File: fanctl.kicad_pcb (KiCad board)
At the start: 4 copper layers, 37.8 x 25 mm, 28 parts, among them U1 74LVC2G17, U2 74LVC2G17

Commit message: release candidate
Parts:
- removed R1, R2, R3: 0R, Resistor_SMD:R_0603_1608Metric_Pad0.98x0.95mm_HandSolder
- removed RPI1: Conn_01x05, Connector_PinHeader_2.54mm:PinHeader_1x05_P2.54mm_Horizontal
- removed SUP1: Conn_01x02, Connector_PinHeader_2.54mm:PinHeader_1x02_P2.54mm_Horizontal
- added D8: LTST-C191TBKT, Diode_SMD:D_0402_1005Metric_Pad0.77x0.64mm_HandSolder, F.Cu at (81.8, 77.0)
- added J1: Raspberry_Pi_4, Connector_PinSocket_2.54mm:PinSocket_2x20_P2.54mm_Horizontal, F.Cu at (35.1, 87.4)
- added J4: Raspberry_Pi_4, Connector_PinHeader_2.54mm:PinHeader_2x20_P2.54mm_Vertical, F.Cu at (35.1, 83.8)
- added R13: 510K, Resistor_SMD:R_0603_1608Metric_Pad0.98x0.95mm_HandSolder, F.Cu at (69.8, 77.0)
- added R14: 0R, Resistor_SMD:R_0603_1608Metric_Pad0.98x0.95mm_HandSolder, F.Cu at (75.8, 77.0)
- added R15: 0R, Resistor_SMD:R_0603_1608Metric_Pad0.98x0.95mm_HandSolder, F.Cu at (72.8, 77.0)
- added R16: 1K, Resistor_SMD:R_0603_1608Metric_Pad0.98x0.95mm_HandSolder, F.Cu at (78.8, 77.0)
- added R18: 0R, Resistor_SMD:R_0603_1608Metric_Pad0.98x0.95mm_HandSolder, F.Cu at (45.8, 77.0)
- added R19: 0R, Resistor_SMD:R_0603_1608Metric_Pad0.98x0.95mm_HandSolder, F.Cu at (42.8, 77.0)
- C1, C2: footprint Capacitor_SMD:C_0603_1608Metric_Pad1.08x0.95mm_HandSolder -> Capacitor_SMD:C_0805_2012Metric_Pad1.18x1.45mm_HandSolder
- G***: moved to F.Cu
- U1, U2: value 74LVC2G17 -> SN74HCT125DR; footprint Package_TO_SOT_SMD:SOT-23-6_Handsoldering -> Package_SO:SOIC-14_3.9x8.7mm_P1.27mm
- moved G*** 81.7 mm to (68.2, 46.0), turned to 0 degrees
- moved FAN1 74.6 mm to (38.0, 47.8), turned to 180 degrees
- moved FAN2 74.5 mm to (38.1, 60.0), turned to 180 degrees
- moved D4 65.0 mm to (42.8, 59.0), turned to -90 degrees
- moved D6 65.0 mm to (42.8, 52.0), turned to 180 degrees
- moved D1 64.9 mm to (42.8, 47.0), turned to -90 degrees
- moved D5 64.8 mm to (42.8, 40.0), turned to 180 degrees
- moved R9 62.7 mm to (47.8, 52.0), turned to 180 degrees
- moved R6 62.4 mm to (47.8, 40.0), turned to 180 degrees
- moved C1 60.2 mm to (47.8, 47.0), turned to -90 degrees
- moved R7 59.2 mm to (42.8, 43.0), turned to 0 degrees
- moved C2 57.4 mm to (47.8, 59.0), turned to -90 degrees
- moved R10 57.0 mm to (42.8, 55.0), turned to 0 degrees
- moved D2 56.9 mm to (42.8, 67.0)
- moved R8 56.9 mm to (47.8, 43.0), turned to 0 degrees
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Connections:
- U1 pad 1: PWM_CTL_3V3 -> GND
- U1 pad 2: GND -> PWM_FAN_CTL_3V3
- U1 pad 3: GND -> PWM_CTL_5V
- U1 pad 4: unconnected-(U1-Pad4) -> GND
- U1 pad 5: +5V -> PWM0_3V3
- U1 pad 6: PWM_CTL_5V -> Net-(R16-Pad1)
- U2 pad 1: Net-(R10-Pad2) -> GND
- U2 pad 2: GND -> Net-(R7-Pad2)
- U2 pad 3: Net-(R7-Pad2) -> TACH1_3V3
- U2 pad 4: TACH1_3V3 -> GND
- U2 pad 5: +3.3V -> Net-(R10-Pad2)
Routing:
- net +3.3V: track 17.8 -> 131.6 mm, vias 1 -> 3
- net GND: track 25.4 -> 109.2 mm, vias 46 -> 81
- net PWM_CTL_3V3: track 35.9 -> 0.00 mm
- net +5V: track 82.0 -> 115.3 mm, vias 6 -> 2
- net PWM_CTL_5V: track 45.3 -> 71.5 mm, vias 0 -> 3
- net TACH1_3V3: track 30.2 -> 50.4 mm
- net TACH2_5V: track 18.4 -> 3.59 mm
- net TACH1_5V: track 18.1 -> 4.29 mm
- net Net-(J1-GPIO15/UART_RXD): track 0.00 -> 13.3 mm
- net Net-(J1-GPIO12/PWM0): track 0.00 -> 13.3 mm
- net Net-(J1-GPIO14/UART_TXD): track 0.00 -> 13.3 mm
- net PWM_FAN_CTL_3V3: track 0.00 -> 11.3 mm
- net Net-(J1-GPIO13/PWM1): track 0.00 -> 10.7 mm
- net Net-(J1-GPIO20/SPI1_MOSI/PCM_DIN/PWM1): track 0.00 -> 9.62 mm
- net Net-(J1-~{CE0}_SPI0/GPIO08): track 0.00 -> 9.62 mm
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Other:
- board size 37.8 x 25 mm -> 51 x 64 mm
- board text added: "${TITLE} ${REVISION} 01/25 5V FANS ONLY"
- board text added: "CTL"
- board text added: "PWR"
- board text removed: "5V"
- board text removed: "5V FANS"
- board text removed: "PWM"
- board text removed: "rPi_fan_ctl v0.1.1 01/25"
- board text removed: "regensberry"

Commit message: review feedback
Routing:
- net PWM_CTL_5V: track 71.5 -> 72.0 mm
- net GND: vias 81 -> 82
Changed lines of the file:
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@@
 		(title "rPi-fanctl")
 		(date "2025-01-18")
-		(rev "v0.2.0")
+		(rev "v0.2.1")
 	)
 	(layers
@@
 		)
 		(property "Value" "1K"
-			(at 0 1.43 360)
+			(at 0 1.43 0)
 			(layer "F.Fab")
 			(effects
@@
 		)
 		(fp_text user "${REFERENCE}"
-			(at 0 0 360)
+			(at 0 0 0)
 			(layer "F.Fab")
 			(effects
@@
 		)
 		(property "Value" "Conn_01x04"
-			(at 4.385 9.89 360)
+			(at 4.385 9.89 0)
 			(layer "F.Fab")
 			(effects
@@
 		)
 		(property "Value" "1K"
-			(at 0 1.43 360)
+			(at 0 1.43 0)
 			(layer "F.Fab")
 			(effects
@@
 		)
 		(fp_text user "${REFERENCE}"
-			(at 0 0 360)
+			(at 0 0 0)
 			(layer "F.Fab")
 			(effects
@@
 		(tags "resistor handsolder")
 		(property "Reference" "R11"
-			(at 0 -1.43 360)
+			(at 0 -1.43 0)
 			(layer "F.SilkS")
 			(effects
@@
 		)
 		(property "Value" "33K"
-			(at 0 1.43 360)
+			(at 0 1.43 0)
 			(layer "F.Fab")
 			(effects
@@
 		)
 		(fp_text user "${REFERENCE}"
-			(at 0 0 360)
+			(at 0 0 0)
 			(layer "F.Fab")
 			(effects
@@
 		)
 		(property "Value" "0u1"
-			(at 0 1.43 360)
+			(at 0 1.43 0)
 			(layer "F.Fab")
 			(effects
@@
 		)
 		(fp_text user "${REFERENCE}"
-			(at 0 0 360)
+			(at 0 0 0)
 			(layer "F.Fab")
 			(effects
@@
 		(tags "resistor handsolder")
 		(property "Reference" "R4"
-			(at 0 -1.43 360)
+			(at 0 -1.43 0)
 			(layer "F.SilkS")
 			(effects
@@
 		)
 		(property "Value" "1K"
-			(at 0 1.43 360)
+			(at 0 1.43 0)
 			(layer "F.Fab")
 			(effects
@@
 		)
 		(fp_text user "${REFERENCE}"
-			(at 0 0 360)
+			(at 0 0 0)
 			(layer "F.Fab")
 			(effects
@@
 		)
 		(property "Value" "LTST-C191TBKT"
-			(at 0 1.17 360)
+			(at 0 1.17 0)
 			(layer "F.Fab")
 			(effects
@@
 		)
 		(fp_text user "${REFERENCE}"
-			(at 0 0 360)
+			(at 0 0 0)
 			(layer "F.Fab")
 			(effects
@@
 		(tags "resistor handsolder")
 		(property "Reference" "R10"
-			(at 0 -1.43 360)
+			(at 0 -1.43 0)
 			(layer "F.SilkS")
 			(effects
@@
 		)
 		(property "Value" "18K"
-			(at 0 1.43 360)
+			(at 0 1.43 0)
 			(layer "F.Fab")
 			(effects
@@
 		)
 		(fp_text user "${REFERENCE}"
-			(at 0 0 360)
+			(at 0 0 0)
 			(layer "F.Fab")
 			(effects
@@
 		(tags "Through hole angled socket strip THT 2x20 2.54mm double row")
 		(property "Reference" "J1"
-			(at -5.65 -2.77 90)
+			(at -7.54 2.5 90)
 			(layer "F.SilkS")
 			(effects
@@
 		)
 		(fp_text user "${REFERENCE}"
-			(at -8.315 24.13 360)
+			(at -8.315 24.13 0)
 			(layer "F.Fab")
 			(effects
@@
 		(tags "Through hole pin header THT 2x20 2.54mm double row")
 		(property "Reference" "J4"
-			(at 1.27 -2.33 90)
+			(at -8.96 2.6 90)
 			(layer "F.SilkS")
 			(effects
@@
 		)
 		(fp_text user "${REFERENCE}"
-			(at 1.27 24.13 360)
+			(at 1.27 24.13 0)
 			(layer "F.Fab")
 			(effects
@@
 		)
 		(property "Value" "Conn_01x04"
-			(at 4.385 9.89 360)
+			(at 4.385 9.89 0)
 			(layer "F.Fab")
 			(effects
@@
 		(tags "diode handsolder")
 		(property "Reference" "D2"
-			(at 0 -1.17 360)
+			(at 0 -1.17 0)
 			(layer "F.SilkS")
 			(effects
@@
 		)
 		(property "Value" "LTST-C191TBKT"
-			(at 0 1.17 360)
+			(at 0 1.17 0)
 			(layer "F.Fab")
 			(effects
@@
 		)
 		(fp_text user "${REFERENCE}"
-			(at 0 0 360)
+			(at 0 0 0)
 			(layer "F.Fab")
 			(effects
@@
 		)
 		(property "Value" "LTST-C191TBKT"
-			(at 0 1.17 360)
+			(at 0 1.17 0)
 			(layer "F.Fab")
 			(effects
@@
 		)
 		(fp_text user "${REFERENCE}"
-			(at 0 0 360)
+			(at 0 0 0)
 			(layer "F.Fab")
 			(effects
@@
 		(tags "SOIC SO")
 		(property "Reference" "U2"
-			(at 0 -5.28 360)
+			(at 0 -5.28 0)
 			(layer "F.SilkS")
 			(effects
@@
 		)
 		(property "Value" "SN74HCT125DR"
-			(at 0 5.28 360)
+			(at 0 5.28 0)
 			(layer "F.Fab")
 			(effects
@@
 		)
 		(property "Footprint" "Package_SO:SOIC-14_3.9x8.7mm_P1.27mm"
-			(at 0 0 360)
+			(at 0 0 0)
 			(layer "F.Fab")
 			(hide yes)
@@
 		)
 		(property "Datasheet" "https://www.ti.com/general/docs/suppproductinfo.tsp?distId=10&gotoUrl=https%3A%2F%2Fwww.ti.com%2Flit%2Fgpn%2Fsn74hct125"
-			(at 0 0 360)
+			(at 0 0 0)
 			(layer "F.Fab")
 			(hide yes)
@@
 		)
 		(property "Description" "IC BUF NON-INVERT 5.5V 14SOIC"
-			(at 0 0 360)
+			(at 0 0 0)
 			(layer "F.Fab")
 			(hide yes)
@@
 		)
 		(fp_text user "${REFERENCE}"
-			(at 0 0 360)
+			(at 0 0 0)
 			(layer "F.Fab")
 			(effects
@@
 	)
 	(via
-		(at 40.25 44)
-		(size 0.8)
-		(drill 0.4)
-		(layers "F.Cu" "B.Cu")
-		(free yes)
-		(net 1)
-	)
-	(via
 		(at 71.25 70.5)
 		(size 0.8)
@@
 	)
 	(via
-		(at 45.25 44)
+		(at 45.25 44.1)
 		(size 0.8)
 		(drill 0.4)
@@
 	)
 	(via
-		(at 61.25 71)
+		(at 74.25 79)
+		(size 0.8)
+		(drill 0.4)
+		(layers "F.Cu" "B.Cu")
+		(free yes)
+		(net 1)
+	)
+	(via
+		(at 60.25 70.5)
 		(size 0.8)
 		(drill 0.4)
@@
 	)
 	(via
-		(at 40.25 56)
+		(at 40.25 44.1)
 		(size 0.8)
 		(drill 0.4)
@@
 	)
 	(via
+		(at 68.15 78.3)
+		(size 0.8)
+		(drill 0.4)
+		(layers "F.Cu" "B.Cu")
+		(free yes)
+		(net 1)
+	)
+	(via
 		(at 58.75 75)
 		(size 0.8)
@@
 	)
 	(segment
-		(start 40.75 72)
-		(end 46.25 72)
-		(width 0.25)
-		(layer "F.Cu")
-		(net 5)
-	)
-	(segment
 		(start 41.8375 65)
 		(end 40.25 65)
@@
 	)
 	(segment
-		(start 40.25 65.5)
-		(end 40.25 71.5)
+		(start 40.75 72)
+		(end 46.25 72)
 		(width 0.25)
 		(layer "F.Cu")
@@
 		(width 0.25)
 		(layer "F.Cu")
+		(net 5)
+	)
+	(segment
+		(start 40.25 65)
+		(end 40.25 71.5)
+		(width 0.25)
+		(layer "F.Cu")

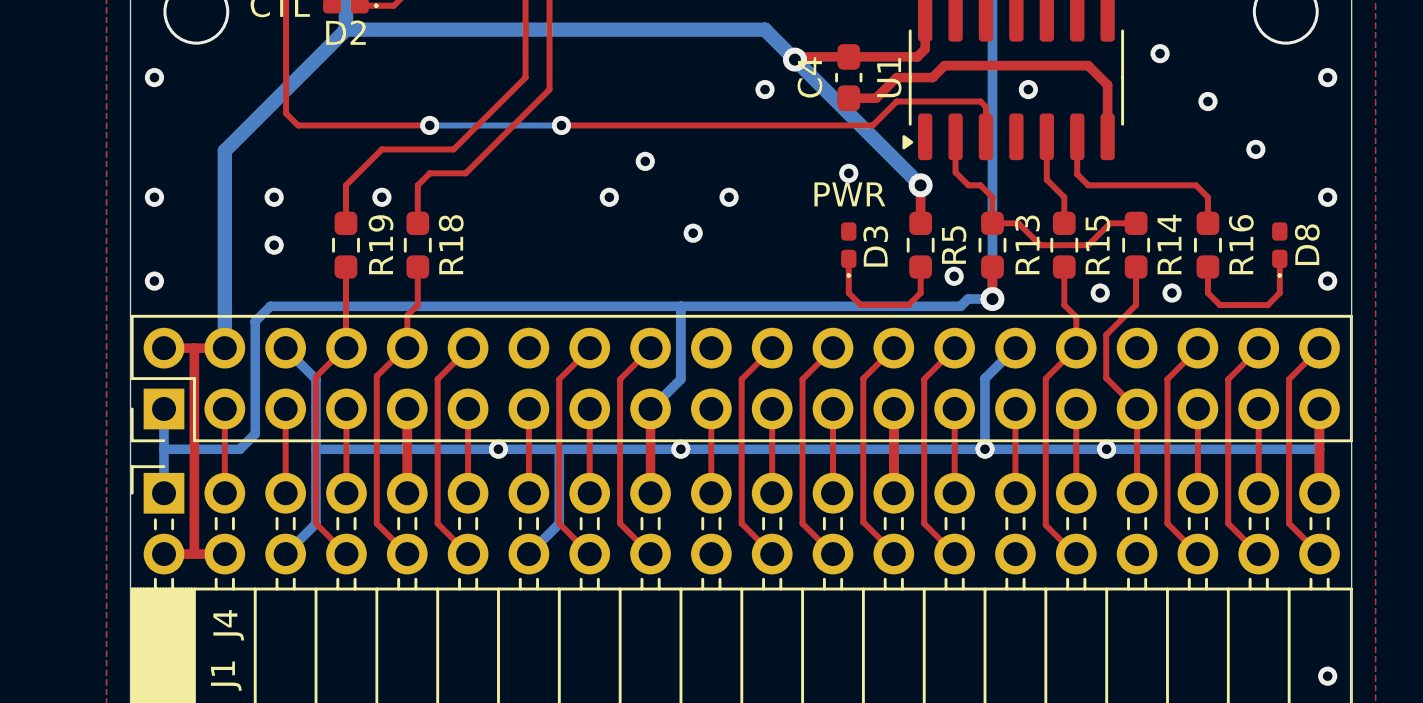
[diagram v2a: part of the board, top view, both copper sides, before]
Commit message: rotated pin headers so they are actually right
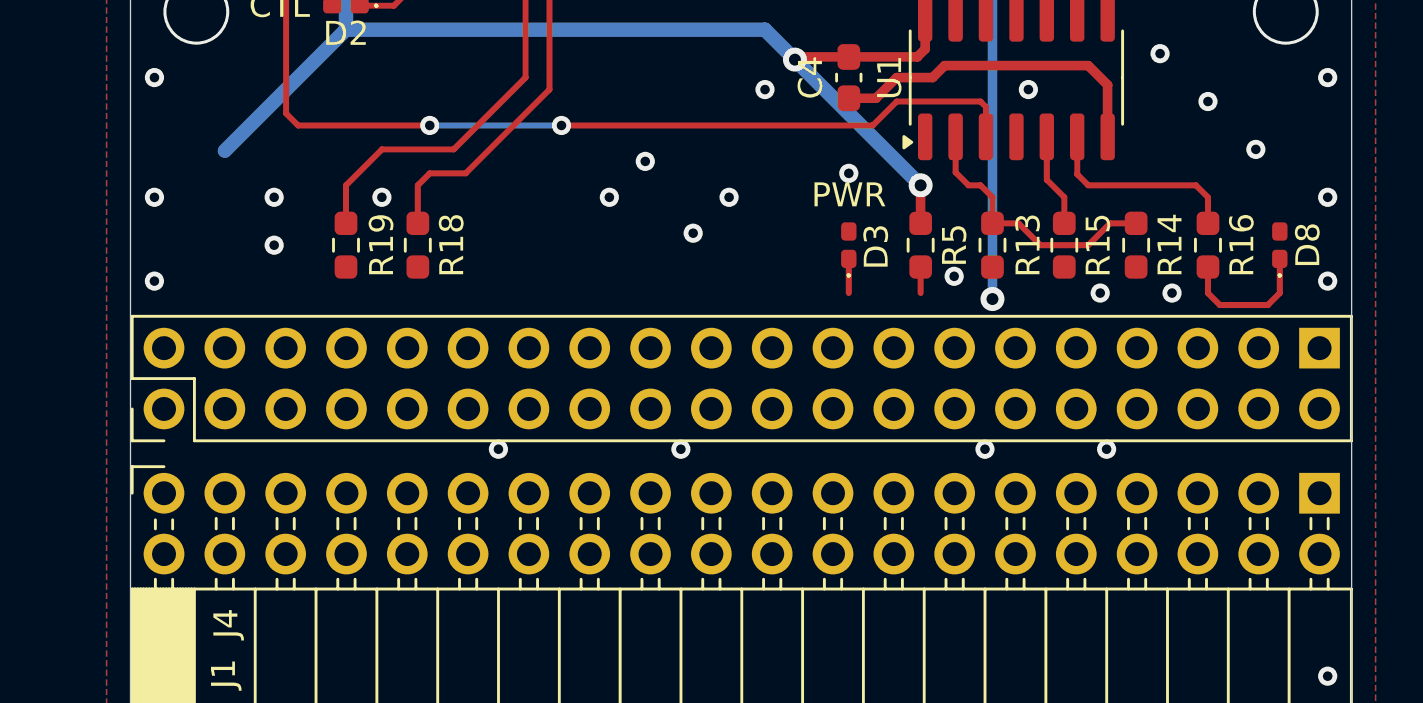
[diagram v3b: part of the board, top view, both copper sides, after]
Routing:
- net GND: track 109.2 -> 27.0 mm
- net +3.3V: track 131.6 -> 77.7 mm
- net +5V: track 115.3 -> 93.4 mm
- net Net-(J1-GPIO15/UART_RXD): track 13.3 -> 0.00 mm
- net Net-(J1-GPIO12/PWM0): track 13.3 -> 0.00 mm
- net Net-(J1-GPIO14/UART_TXD): track 13.3 -> 0.00 mm
- net Net-(J1-GPIO13/PWM1): track 10.7 -> 0.00 mm
- net Net-(J1-GPIO20/SPI1_MOSI/PCM_DIN/PWM1): track 9.62 -> 0.00 mm
- net Net-(J1-~{CE0}_SPI0/GPIO08): track 9.62 -> 0.00 mm
- net Net-(J1-GPIO23/SDIO_CMD): track 9.62 -> 0.00 mm
- net Net-(J1-GPIO18/SPI1_~{CE0}/PCM_CLK/PWM0): track 9.62 -> 0.00 mm
- net Net-(J1-GPIO24/SDIO_DAT0): track 9.62 -> 0.00 mm
- net Net-(J1-GPIO21/SPI1_SCLK/PCM_DOUT): track 9.62 -> 0.00 mm
- net Net-(J1-GPIO16/SPI1_~{CE2}): track 9.62 -> 0.00 mm
- net Net-(J1-ID_SC_I2C0/GPIO01): track 9.62 -> 0.00 mm
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
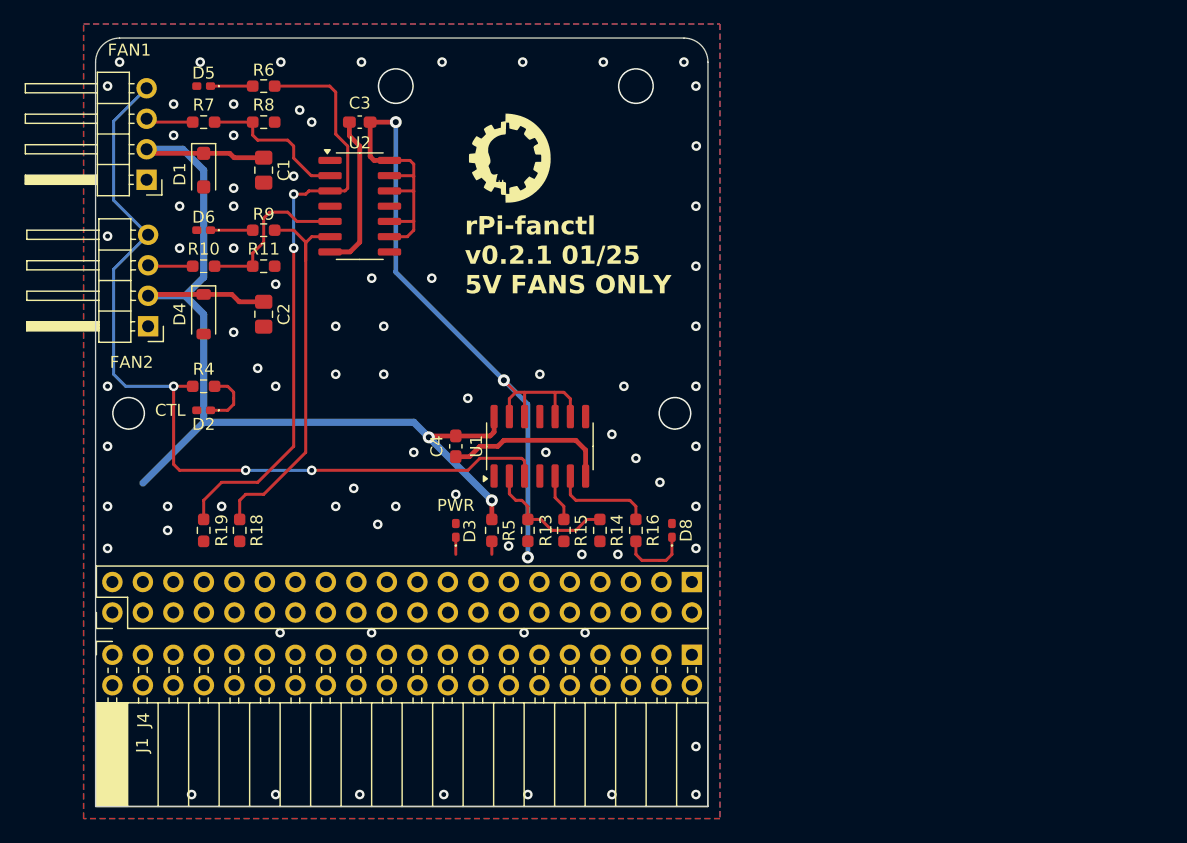
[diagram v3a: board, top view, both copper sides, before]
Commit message: connectors corrected
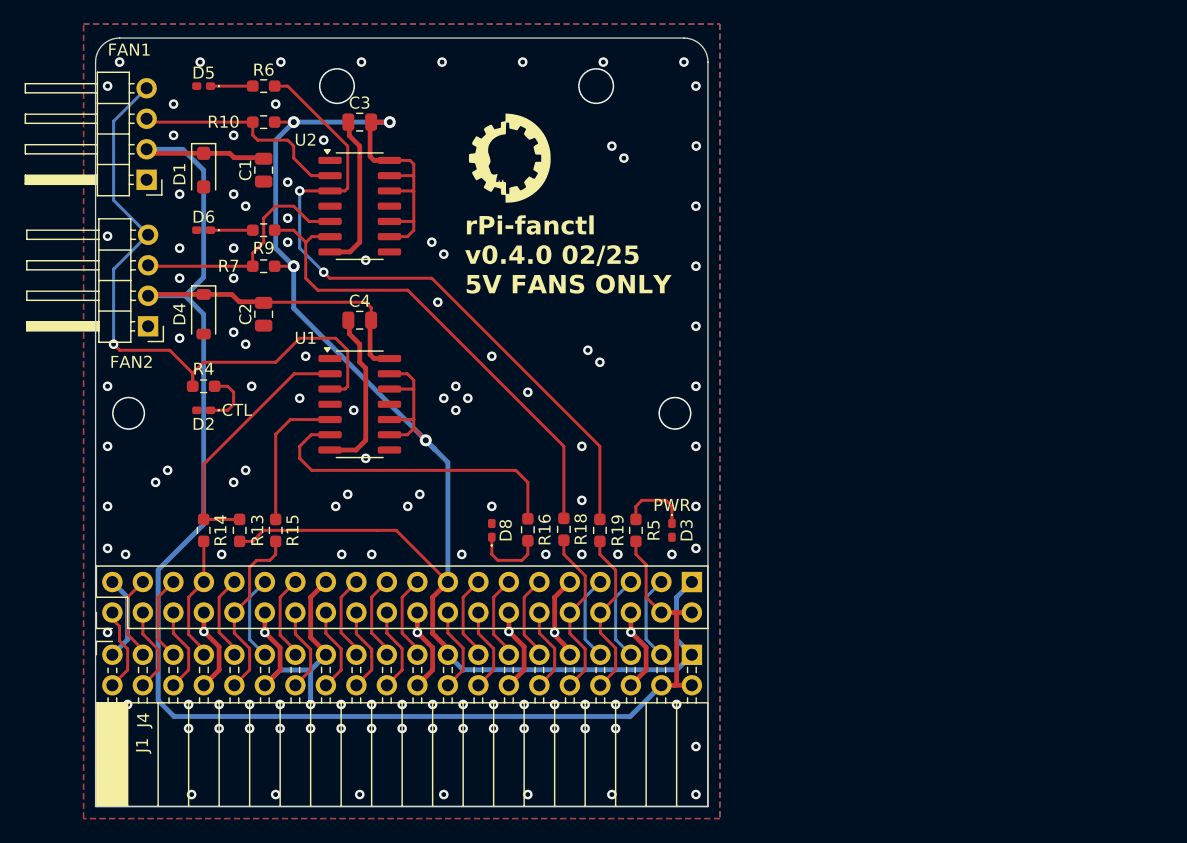
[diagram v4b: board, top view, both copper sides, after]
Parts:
- removed R11, R8: 33K, Resistor_SMD:R_0603_1608Metric_Pad0.98x0.95mm_HandSolder
- C1, C2: footprint Capacitor_SMD:C_0805_2012Metric_Pad1.18x1.45mm_HandSolder -> Capacitor_SMD:C_0805_2012Metric
- C3, C4: footprint Capacitor_SMD:C_0603_1608Metric_Pad1.08x0.95mm_HandSolder -> Capacitor_SMD:C_0805_2012Metric
- R10, R7: value 18K -> 10K
- R14, R15, R18, R19: value 0R -> 120R
- moved R14 33.0 mm to (42.8, 77.0)
- moved R19 33.0 mm to (75.8, 77.0)
- moved R18 27.0 mm to (72.8, 76.9)
- moved R13 24.0 mm to (45.8, 77.0)
- moved R15 24.0 mm to (48.8, 77.0)
- moved D3 18.0 mm to (81.8, 77.0), turned to -90 degrees
- moved U1 15.4 mm to (55.8, 66.5), turned to 0 degrees
- moved D8 15.0 mm to (66.8, 77.0)
- moved C4 13.2 mm to (55.8, 59.5), turned to 180 degrees
- moved R10 13.0 mm to (47.8, 43.0), turned to 180 degrees
- moved R7 13.0 mm to (47.8, 55.0), turned to 180 degrees
- moved R5 12.0 mm to (78.8, 77.0), turned to 90 degrees
- moved R16 9.00 mm to (69.8, 77.0)
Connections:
- FAN1 pad 3: TACH1_5V -> TACH1
- FAN2 pad 3: TACH2_5V -> TACH2
- R10 pad 1: TACH2_5V -> +3.3V
- R10 pad 2: Net-(R10-Pad2) -> TACH1
- R7 pad 1: TACH1_5V -> +3.3V
- R7 pad 2: Net-(R7-Pad2) -> TACH2
- U2 pad 2: Net-(R7-Pad2) -> TACH1
- U2 pad 5: Net-(R10-Pad2) -> TACH2
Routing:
- net +3.3V: track 77.7 -> 148.6 mm, vias 3 -> 4
- net GND: track 27.0 -> 92.9 mm, vias 82 -> 133
- net +5V: track 93.4 -> 152.0 mm, vias 2 -> 0
- net TACH2: track 0.00 -> 19.4 mm
- net TACH1: track 0.00 -> 18.8 mm
- net PWM_CTL_5V: track 72.0 -> 53.5 mm, vias 3 -> 1
- net Net-(R16-Pad1): track 8.51 -> 26.8 mm
- net Net-(J1-GPIO12/PWM0): track 0.00 -> 15.1 mm
- net Net-(J1-GPIO15/UART_RXD): track 0.00 -> 14.4 mm
- net Net-(J1-GPIO14/UART_TXD): track 0.00 -> 14.1 mm
- net Net-(R10-Pad2): track 13.5 -> 0.00 mm
- net Net-(R7-Pad2): track 12.6 -> 0.00 mm
- net Net-(J1-GPIO13/PWM1): track 0.00 -> 10.4 mm
- net PWM_FAN_CTL_3V3: track 11.3 -> 21.4 mm
- net TACH2_3V3: track 32.9 -> 41.5 mm
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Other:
- board text added: "${TITLE} ${REVISION} 02/25 5V FANS ONLY"
- board text removed: "${TITLE} ${REVISION} 01/25 5V FANS ONLY"

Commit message: added lines to align fan connector
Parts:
- moved D2 40.4 mm to (77.2, 46.0), turned to 90 degrees
- moved R4 37.2 mm to (74.8, 46.0), turned to -90 degrees
- moved FAN2 0.08 mm to (38.0, 60.0)
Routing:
- net PWM_CTL_5V: track 53.5 -> 91.8 mm, vias 1 -> 2
- net +3.3V: track 148.6 -> 149.8 mm
- net Net-(D2-Pad1): track 5.00 -> 5.50 mm
- net GND: vias 133 -> 135
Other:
- board text added: "FANCTL"
- board text removed: "CTL"
